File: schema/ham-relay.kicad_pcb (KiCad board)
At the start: 2 copper layers, 140 x 98 mm, 69 parts, among them J1 DB9, P1 JTAG, P2 CONN_01X08, P3 RESET, P4 ISP, P5 CONN_01X03, U1 REG3V3, U2 CPC1017N, U3 LPC1114FN28/102, U4 XYZ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

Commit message: Routing
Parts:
- moved R31 78.6 mm to (142.9, 48.3)
- moved R23 52.2 mm to (149.2, 87.0), turned to 270 degrees
- moved R10 33.7 mm to (159.4, 123.8)
- moved R12 30.1 mm to (186.7, 119.4)
- moved R2 28.5 mm to (80.0, 103.5)
- moved R9 10.0 mm to (157.5, 92.1), turned to 0 degrees
- moved R11 4.58 mm to (101.6, 54.6), turned to 180 degrees
- moved R19 3.70 mm to (157.5, 87.6)
- moved R16 2.29 mm to (186.7, 114.9), turned to 180 degrees
- moved C7 1.91 mm to (165.1, 123.2)
- moved R29 1.91 mm to (122.6, 51.4)
- moved R7 1.91 mm to (158.1, 70.5)
- moved U2 1.91 mm to (160.0, 95.2)
- moved R13 1.27 mm to (80.0, 117.5)
- moved R27 1.27 mm to (118.7, 62.2)
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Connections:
- P2 pad 6: /Audio/AUDIO_OUT -> GND
- P2 pad 7: (no net) -> /Audio/AUDIO_OUT
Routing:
- net +3V3: track 0.00 -> 256.2 mm, vias 0 -> 1
- net VCC: track 0.00 -> 218.4 mm, vias 0 -> 2
- net /RX_CR: track 0.00 -> 178.1 mm
- net /TONE_SW: track 0.00 -> 138.3 mm
- net /TXE: track 0.00 -> 132.5 mm
- net /SWCLK: track 0.00 -> 127.7 mm, vias 0 -> 1
- net /SWO: track 0.00 -> 123.2 mm, vias 0 -> 3
- net /SWDIO: track 0.00 -> 87.8 mm, vias 0 -> 1
- net /Audio/TONE: track 0.00 -> 76.8 mm, vias 0 -> 1
- net Net-(R18-Pad1): track 0.00 -> 75.2 mm, vias 0 -> 1
- net /RESET: track 0.00 -> 72.2 mm, vias 0 -> 2
- net /Audio/AUDIO_OUT: track 0.00 -> 66.5 mm, vias 0 -> 1
- net /EXT: track 0.00 -> 66.5 mm
- net /RXE: track 0.00 -> 62.7 mm
- net /Audio/AUDIO_IN: track 0.00 -> 61.9 mm
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- added copper zone on B.Cu, net GND
- added copper zone on F.Cu, net GND
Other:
- net class VCC added: clearance 0.4064, trace_width 1.016, via_dia 1.5, via_drill 0.5

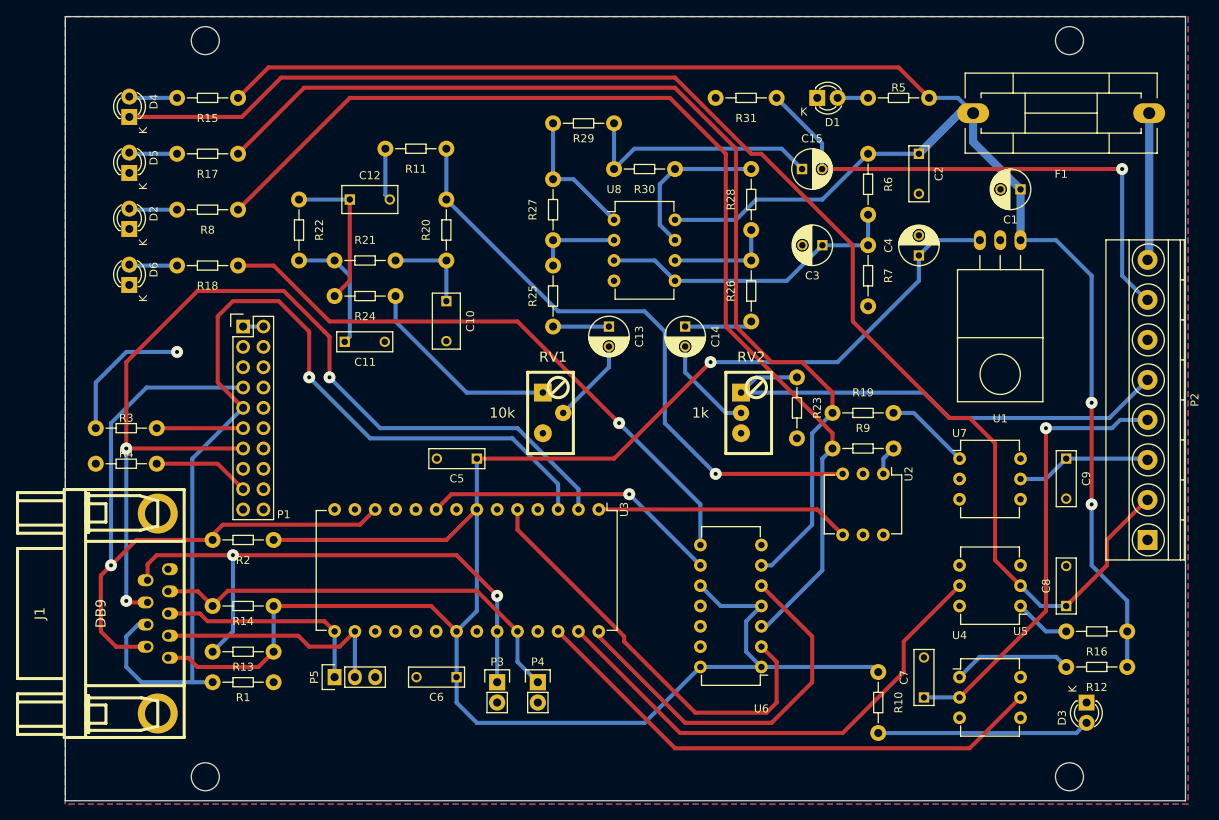
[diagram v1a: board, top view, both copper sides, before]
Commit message: * Add EXT LED * Silkscreen
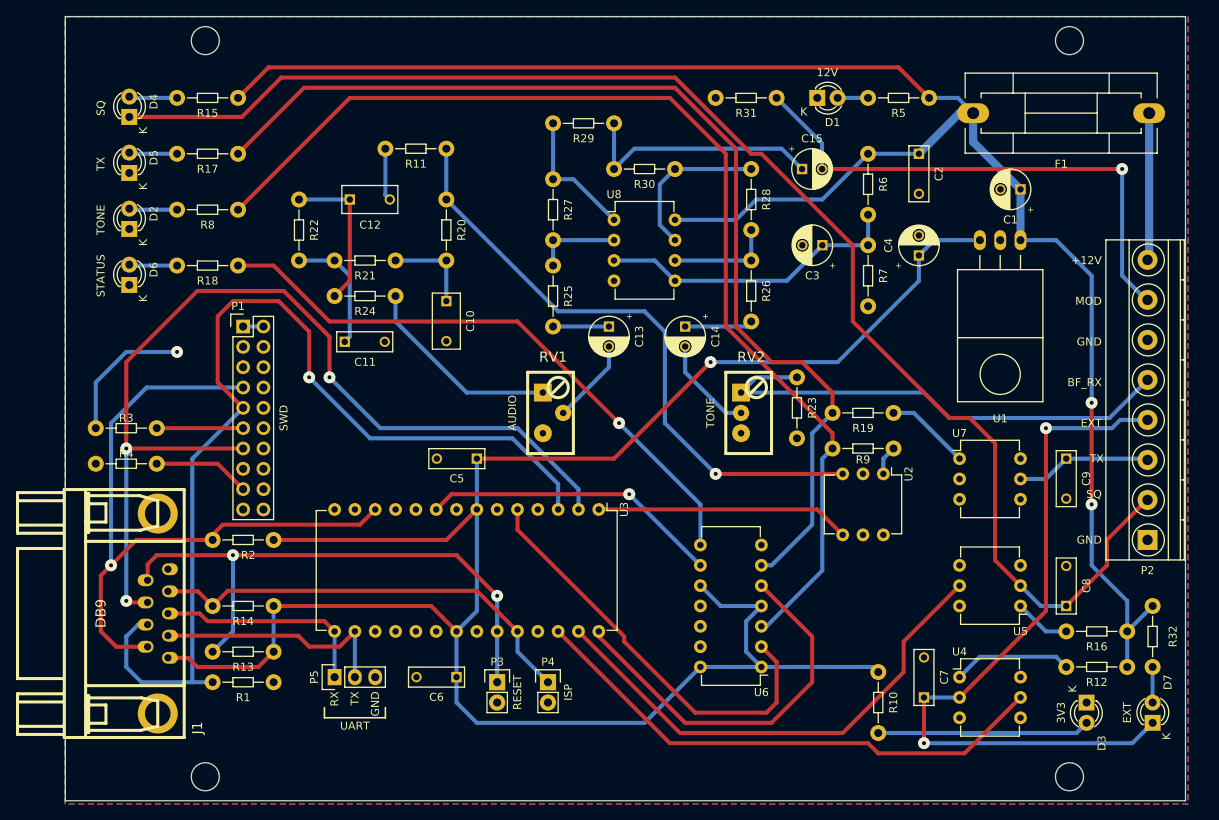
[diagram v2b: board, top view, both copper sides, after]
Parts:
- added D7: RX, LEDs:LED-3MM, F.Cu at (193.7, 126.4)
- added R32: ?, resistors:Resistor_Horizontal_RM08mm, F.Cu at (193.7, 115.6)
- moved P4 1.27 mm to (118.1, 121.3)
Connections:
- P1 pad 15: (no net) -> Net-(P1-Pad15)
- P1 pad 19: (no net) -> Net-(P1-Pad19)
- P1 pad 3: (no net) -> Net-(P1-Pad3)
- P1 pad 5: (no net) -> Net-(P1-Pad5)
- U3 pad 10: (no net) -> Net-(U3-Pad10)
- U3 pad 11: (no net) -> Net-(U3-Pad11)
- U3 pad 13: (no net) -> Net-(U3-Pad13)
- U3 pad 14: (no net) -> Net-(U3-Pad14)
- U3 pad 17: (no net) -> Net-(U3-Pad17)
- U3 pad 18: (no net) -> Net-(U3-Pad18)
- U3 pad 19: (no net) -> Net-(U3-Pad19)
- U3 pad 25: (no net) -> Net-(U3-Pad25)
- U3 pad 4: (no net) -> Net-(U3-Pad4)
- U3 pad 6: (no net) -> Net-(U3-Pad6)
- U4 pad 6: (no net) -> Net-(U4-Pad6)
- U5 pad 6: (no net) -> Net-(U5-Pad6)
- U7 pad 6: (no net) -> Net-(U7-Pad6)
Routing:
- net /EXT_CR: track 55.7 -> 91.0 mm, vias 1 -> 2
- net VCC: track 218.4 -> 223.5 mm
- net Net-(D7-Pad2): track 0.00 -> 4.45 mm
- net /EXT: track 66.5 -> 67.0 mm
- net /ISP: track 54.7 -> 55.3 mm
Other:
- board text added: "+"
- board text added: "+12V"
- board text added: "12V"
- board text added: "3V3"
- board text added: "AUDIO"
- board text added: "BF_RX"
- board text added: "EXT"
- board text added: "GND"
- board text added: "ISP"
- board text added: "MOD"
- board text added: "RESET"
- board text added: "RX"
- board text added: "SQ"
- board text added: "STATUS"
- board text added: "SWD"
- board text added: "TONE"
- board text added: "TX"
- board text added: "UART"

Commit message: Missing net
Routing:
- net +3V3: track 256.2 -> 285.0 mm
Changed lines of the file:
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@@
   (general
     (links 162)
-    (no_connects 1)
+    (no_connects 0)
     (area 57.709999 38.024999 197.860001 136.175001)
     (thickness 1.6)
     (drawings 41)
-    (tracks 330)
+    (tracks 333)
     (zones 0)
     (modules 71)
@@
   (segment (start 97.79 54.61) (end 97.79 60.405) (width 0.508) (layer B.Cu) (net 1))
   (segment (start 97.79 60.405) (end 98.345 60.96) (width 0.508) (layer B.Cu) (net 1))
+  (segment (start 83.82 103.505) (end 85.725 101.6) (width 0.508) (layer B.Cu) (net 2))
+  (segment (start 85.725 80.01) (end 82.55 76.835) (width 0.508) (layer B.Cu) (net 2))
+  (segment (start 85.725 101.6) (end 85.725 80.01) (width 0.508) (layer B.Cu) (net 2))
   (segment (start 144.78 111.76) (end 139.7 111.76) (width 0.508) (layer B.Cu) (net 2))
   (segment (start 139.7 111.76) (end 137.16 109.22) (width 0.508) (layer B.Cu) (net 2))

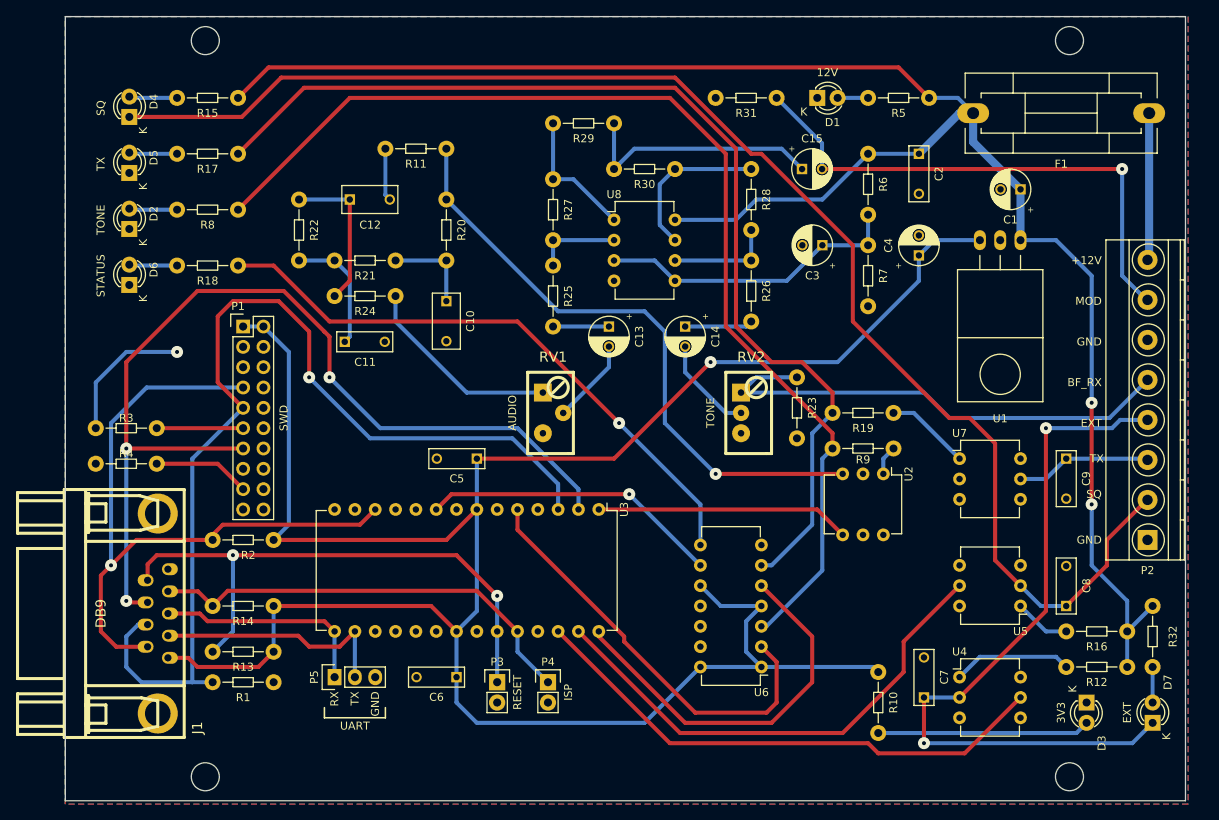
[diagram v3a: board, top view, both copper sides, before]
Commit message: Improve routing for better ground plane and thermal relieved pads
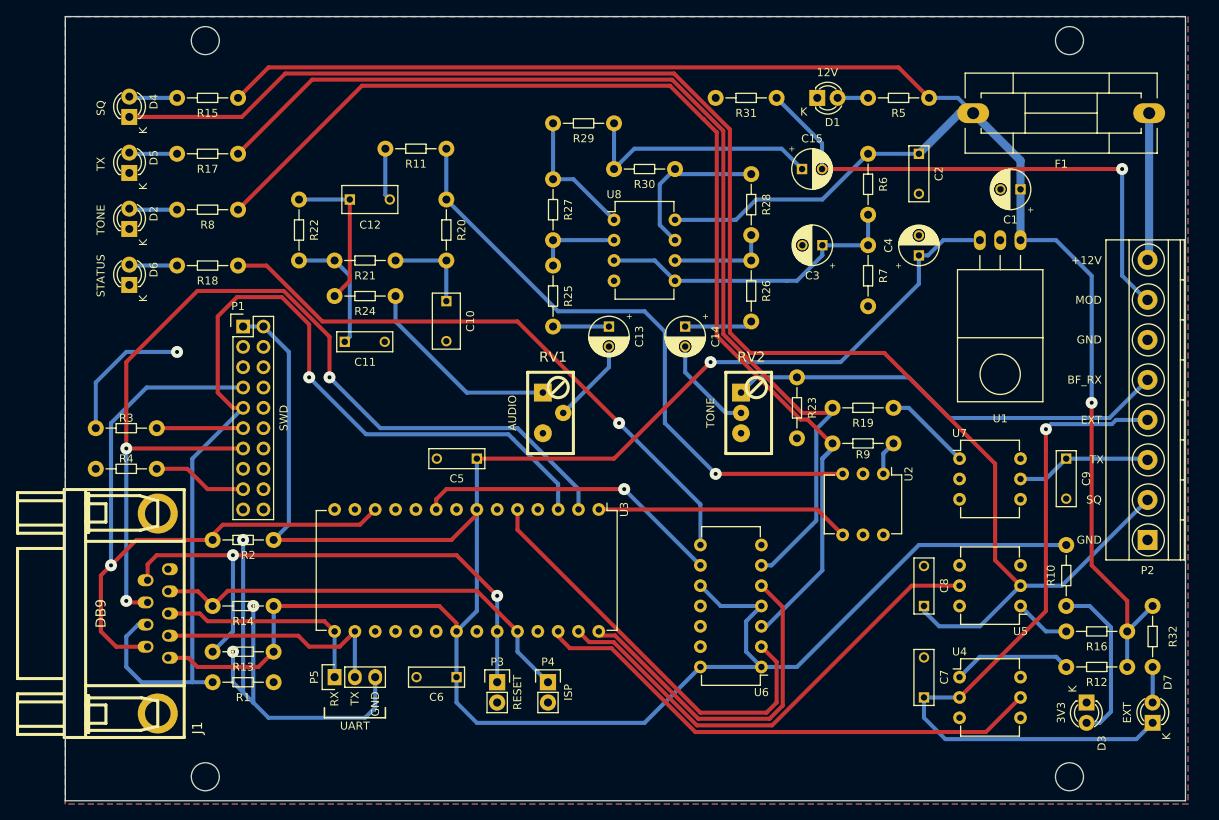
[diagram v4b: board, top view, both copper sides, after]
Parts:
- moved R10 28.4 mm to (182.9, 108.0)
- moved C8 17.8 mm to (165.1, 111.8)
- moved R9 0.64 mm to (157.5, 91.4)
- moved R28 0.63 mm to (143.5, 61.6)
- moved R19 0.63 mm to (157.5, 87.0)
- moved R4 0.63 mm to (65.4, 94.6)
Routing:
- net GND: track 24.0 -> 82.9 mm, vias 1 -> 4
- net +3V3: track 285.0 -> 315.7 mm
- net /RX_CR: track 178.1 -> 198.1 mm
- net /Audio/AUDIO_IN: track 61.9 -> 55.7 mm
- net Net-(D3-Pad2): track 26.6 -> 20.9 mm
- net /TONE_SW: track 138.3 -> 143.2 mm
- net Net-(U3-Pad28): track 48.6 -> 44.4 mm
- net /RXE: track 62.7 -> 59.7 mm
- net /EXT_CR: track 91.0 -> 88.7 mm, vias 2 -> 1
- net Net-(U3-Pad9): track 37.5 -> 39.4 mm
- net /EXT: track 67.0 -> 65.2 mm
- net /SWCLK: track 127.7 -> 129.4 mm
- net /TXE: track 132.5 -> 133.8 mm
- net VCC/2: track 38.5 -> 39.2 mm
- net Net-(R9-Pad2): track 3.70 -> 4.34 mm
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
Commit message: Only missing the holes
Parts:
- added HOLE1: 1pin, Connect:1pin, F.Cu at (174.6, 82.8)
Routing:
- net /SWO: track 123.2 -> 122.3 mm
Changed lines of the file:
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@@
 (kicad_pcb (version 4) (host pcbnew 4.0.1-stable)
   (general
-    (links 162)
+    (links 163)
     (no_connects 0)
     (area 57.709999 38.024999 197.860001 136.175001)
     (thickness 1.6)
     (drawings 41)
-    (tracks 368)
+    (tracks 367)
     (zones 0)
-    (modules 71)
+    (modules 72)
     (nets 71)
   )
   (page A4)
   (layers
-    (0 F.Cu signal)
+    (0 F.Cu signal hide)
     (31 B.Cu signal)
     (32 B.Adhes user)
@@
     (mod_text_size 1 1)
     (mod_text_width 0.15)
-    (pad_size 4.064 4.064)
+    (pad_size 3.35 3.35)
     (pad_drill 3.048)
     (pad_to_mask_clearance 0.2)
@@
     )
   )
-  (gr_text SWD (at 85.09 88.265 90) (layer F.SilkS)
+  (module Connect:1pin (layer F.Cu)
+    (at 174.625 82.804)
+    (descr "module 1 pin (ou trou mecanique de percage)")
+    (tags DEV)
+    (zone_connect 2)
+    (fp_text reference HOLE1 (at 0 -3.048) (layer F.SilkS) hide
+      (effects (font (size 1 1) (thickness 0.15)))
+    )
+    (fp_text value 1pin (at 0 2.794) (layer F.Fab)
+      (effects (font (size 1 1) (thickness 0.15)))
+    )
+    (fp_circle (center 0 0) (end 0 -2.286) (layer F.SilkS) (width 0.15))
+    (pad 1 thru_hole circle (at 0 0) (size 4.064 4.064) (drill 3.048) (layers *.Cu *.Mask F.SilkS)
+      (net 1 GND) (zone_connect 2))
+  )
+  (gr_text SWD (at 77.47 88.265 90) (layer F.SilkS)
     (effects (font (size 1 1) (thickness 0.15)))
   )
@@
   (segment (start 63.5 106.68) (end 62.23 107.95) (width 0.508) (layer F.Cu) (net 23))
   (segment (start 68.072 116.85544) (end 64.15044 116.85544) (width 0.508) (layer F.Cu) (net 23) (status 10))
-  (segment (start 113.7285 90.8685) (end 113.157 90.297) (width 0.508) (layer B.Cu) (net 24))
-  (segment (start 113.157 90.297) (end 95.377 90.297) (width 0.508) (layer B.Cu) (net 24))
+  (segment (start 112.649 90.297) (end 119.38 97.028) (width 0.508) (layer B.Cu) (net 24))
+  (segment (start 112.649 90.297) (end 95.377 90.297) (width 0.508) (layer B.Cu) (net 24))
   (segment (start 88.265 76.581) (end 84.836 73.152) (width 0.508) (layer F.Cu) (net 24))
   (via (at 88.265 83.185) (size 1.5) (drill 0.5) (layers F.Cu B.Cu) (net 24))
@@
   (segment (start 76.835 75.565) (end 79.248 73.152) (width 0.508) (layer F.Cu) (net 24))
   (segment (start 76.835 85.09) (end 76.835 75.565) (width 0.508) (layer F.Cu) (net 24))
-  (segment (start 119.38 96.52) (end 119.38 99.695) (width 0.508) (layer B.Cu) (net 24) (status 20))
-  (segment (start 113.7285 90.8685) (end 119.38 96.52) (width 0.508) (layer B.Cu) (net 24))
+  (segment (start 119.38 97.028) (end 119.38 99.695) (width 0.508) (layer B.Cu) (net 24) (status 20))
   (segment (start 73.66 121.285) (end 73.66 93.345) (width 0.508) (layer B.Cu) (net 24))
   (segment (start 73.66 93.345) (end 80.01 86.995) (width 0.508) (layer B.Cu) (net 24) (status 20))
@@
   (segment (start 65.405 119.38) (end 67.31 121.285) (width 0.508) (layer B.Cu) (net 24))
   (segment (start 65.405 115.57) (end 65.405 119.38) (width 0.508) (layer B.Cu) (net 24))
-  (segment (start 121.92 99.695) (end 121.92 97.155) (width 0.508) (layer B.Cu) (net 25) (status 10))
+  (segment (start 112.903 89.535) (end 121.92 98.552) (width 0.508) (layer B.Cu) (net 25))
+  (segment (start 121.92 99.695) (end 121.92 98.552) (width 0.508) (layer B.Cu) (net 25) (status 10))
   (segment (start 90.805 78.105) (end 90.805 83.185) (width 0.508) (layer F.Cu) (net 25))
   (segment (start 65.405 81.28) (end 65.405 92.075) (width 0.508) (layer F.Cu) (net 25))
@@
   (via (at 90.805 83.185) (size 1.5) (drill 0.5) (layers F.Cu B.Cu) (net 25))
   (segment (start 97.155 89.535) (end 90.805 83.185) (width 0.508) (layer B.Cu) (net 25))
-  (segment (start 114.3 89.535) (end 97.155 89.535) (width 0.508) (layer B.Cu) (net 25))
-  (segment (start 121.92 97.155) (end 114.3 89.535) (width 0.508) (layer B.Cu) (net 25))
+  (segment (start 112.903 89.535) (end 97.155 89.535) (width 0.508) (layer B.Cu) (net 25))
   (segment (start 68.072 111.3157) (end 65.5957 111.3157) (width 0.508) (layer F.Cu) (net 25) (status 10))
   (segment (start 65.405 92.075) (end 80.01 92.075) (width 0.508) (layer F.Cu) (net 25) (status 20))
